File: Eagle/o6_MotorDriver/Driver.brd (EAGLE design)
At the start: 160 x 100 mm, 17 parts, among them IC1 ULN2003AD, IC2 REG1117, P1C2 10uF, P1C3 10uF

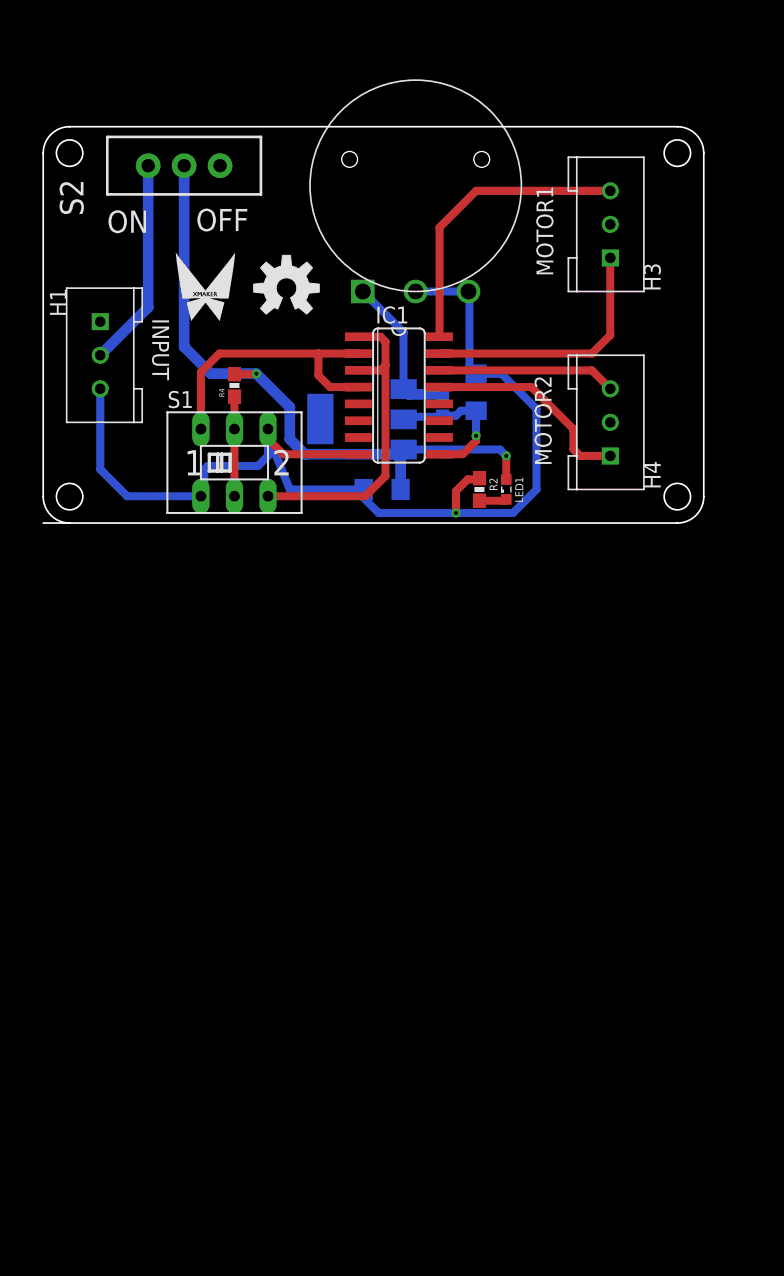
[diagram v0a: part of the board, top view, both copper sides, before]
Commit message: change motordriver
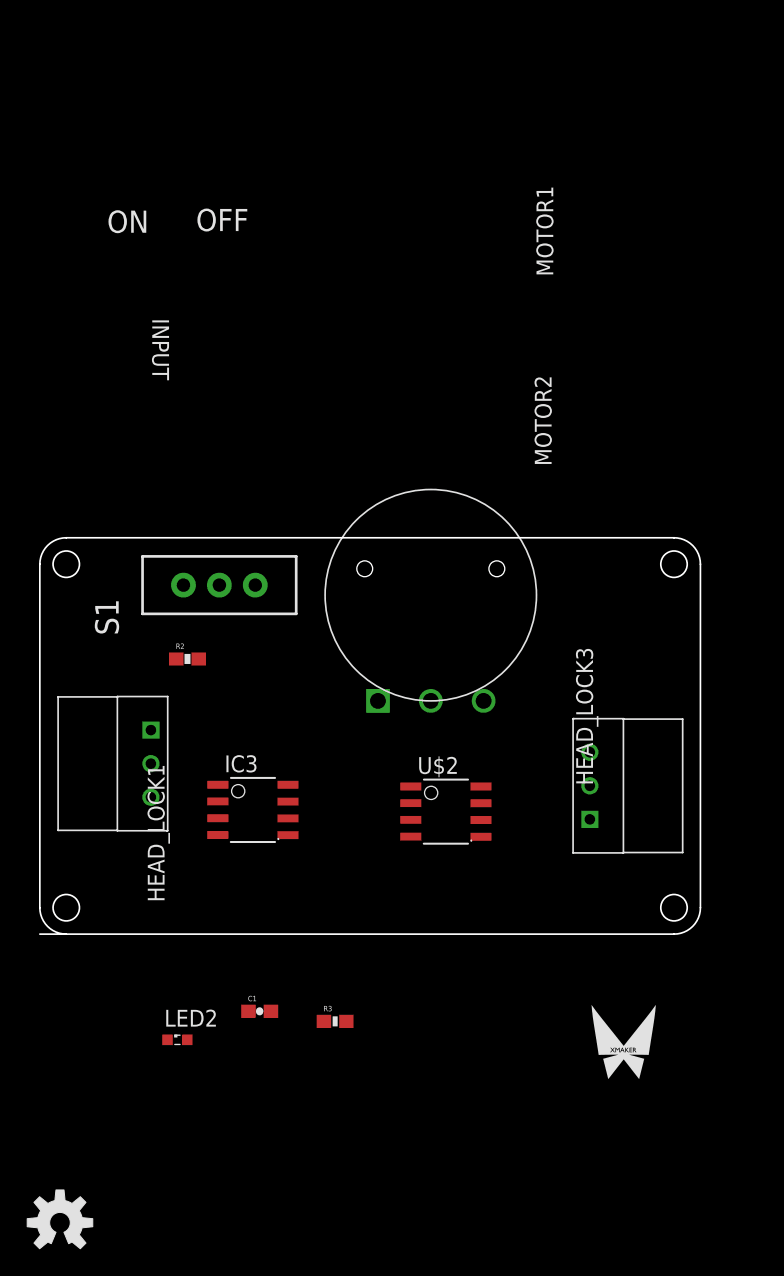
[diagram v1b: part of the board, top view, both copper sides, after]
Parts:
- removed H1, H3, H4: HEAD_LOCK, HEAD_LOCK:HEAD_LOCK
- removed IC1: ULN2003AD, uln-udn:SO16
- removed IC2: REG1117, burr-brown:SOT223
- removed LED1: (no value), eagle-ltspice:LED_SML0603
- removed P1C2, P1C3: 10uF, SparkFun:EIA3216
- removed R1: 121, SparkFun-Resistors:0603-RES
- removed R4: 10K, SparkFun-Resistors:0603-RES
- removed S2: (no value), SparkFun-Electromechanical:SWITCH-SPDT_KIT
- removed U$3: DIMENSION1, Xmaker_yuhui:DIMENSION1
- removed U$4: OPENHARDWARE, Xmaker_yuhui:OPENHARDWARE
- removed U$5: 1K, Xmaker_yuhui:POT_CIRCLE
- added C1: 0.1uF, SparkFun-Passives:0603-CAP
- added HEAD_LOCK1, HEAD_LOCK3: HEAD_LOCK, Xmaker_yuhui:HEAD_LOCK
- added IC3: TINY13-20SSU, atmel:8S1
- added LED2: (no value), eagle-ltspice:LED_SML0603
- added R3: (no value), SparkFun-Resistors:0603-RES
- added U$1: DIMENSION1, Xmaker_yuhui:DIMENSION1
- added U$6: POL_CIRCLE, Xmaker_yuhui:POT_CIRCLE
- added U$7: XMAKERLOGO_5MM_TOP, Xmaker_yuhui:XMAKERLOGO_5MM_TOP
- added U$8: OPENHARDWARE_5MM_TOP, Xmaker_yuhui:OPENSOURCE_5MM_TOP
- R2: device SparkFun-Resistors:0603-RES -> SparkFun-Passives:0603-RES
- S1: device switch:A68-A31 -> SparkFun-Electromechanical:SWITCH-SPDT_KIT
- U$2: value XMAKERLOGO2 -> L9110; device Xmaker_yuhui:XMAKERLOGO2 -> Xmaker_yuhui:SOP8
- moved U$2 42.2 mm to (31.8, -62.5), turned to 270 degrees
- moved R2 25.6 mm to (12.2, -50.9), turned to 0 degrees
- moved S1 9.34 mm to (14.6, -45.3), turned to 90 degrees
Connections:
- removed net IN1: IC1.1, IC1.3, S1.3
- removed net IN2: IC1.2, IC1.4, S1.4
- removed net MOTOR3: H4.1, IC1.13
- removed net MOTOR4: H4.3, IC1.14
- removed net N$1: LED1.C, R2.2
- removed net N$3: IC2.1, R1.1, U$5.P$1
- removed net N$4: H1.2, S2.1
- removed net VOUT: IC1.9, IC2.2, P1C3.A, R1.2
- new net ADC: HEAD_LOCK1.1, IC3.2
- new net DIR: IC3.7, U$2.7
- new net N$5: LED2.C, R3.2
- new net PWM: IC3.5, U$2.6
- new net SELECT: IC3.6, S1.2
- new net SPEED: IC3.3, U$6.P$2
- net GND: now also C1.2, HEAD_LOCK1.3, IC3.4, R3.1, S1.3, U$2.5, U$2.8, U$6.P$3; no longer H1.3, IC1.8, P1C2.C, P1C3.C, R2.1, S1.1, S1.6, U$5.P$2, U$5.P$3
- net MOTOR1: now also HEAD_LOCK3.3, U$2.1; no longer H3.1, IC1.15
- net MOTOR2: now also HEAD_LOCK3.1, U$2.4; no longer H3.3, IC1.16
- net N$2: now also R2.1, S1.1; no longer R4.1, S1.2, S1.5
- net VCC: now also C1.1, HEAD_LOCK1.2, IC3.1, IC3.8, LED2.A, R2.2, U$2.2, U$2.3, U$6.P$1; no longer IC2.3, LED1.A, P1C2.A, R4.2, S2.2
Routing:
- net GND: track 82.9 -> 0.00 mm, vias 1 -> 0
- net VCC: track 48.8 -> 0.00 mm, vias 2 -> 0
- net IN1: track 24.1 -> 0.00 mm
- net MOTOR2: track 22.4 -> 0.00 mm
- net IN2: track 21.9 -> 0.00 mm
- net MOTOR1: track 19.3 -> 0.00 mm
- net MOTOR3: track 16.0 -> 0.00 mm
- net N$4: track 15.9 -> 0.00 mm
- net MOTOR4: track 13.5 -> 0.00 mm
- net N$3: track 11.8 -> 0.00 mm
- net VOUT: track 11.2 -> 0.00 mm, vias 1 -> 0
- net N$2: track 7.53 -> 0.00 mm
- net N$1: track 2.07 -> 0.00 mm

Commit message: gxzz
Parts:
- moved LED2 45.3 mm to (43.7, -48.0), turned to 180 degrees
- moved R3 35.3 mm to (44.2, -49.9)
- moved C1 19.3 mm to (18.4, -58.3)
- moved U$8 11.5 mm to (9.53, -84.5)
- moved IC3 3.18 mm to (20.3, -62.5)
- moved R2 2.33 mm to (10.0, -50.0), turned to 270 degrees
- moved HEAD_LOCK3 2.05 mm to (42.4, -58.5)
- moved S1 1.91 mm to (12.7, -45.5)
- moved U$6 0.90 mm to (30.0, -54.7)
- moved HEAD_LOCK1 0.72 mm to (9.91, -58.3)

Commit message: 12.15
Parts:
- removed HEAD_LOCK1, HEAD_LOCK3: HEAD_LOCK, Xmaker_yuhui:HEAD_LOCK
- added HEAD_LOCK2: HEAD_LOCK, Xmaker:HEAD_LOCK
- added U$4: HEAD_LOCK2, Xmaker:HEAD_LOCK2
- moved U$8 109.5 mm to (9.00, 25.0)
- moved U$7 105.2 mm to (41.0, 25.0)
- moved U$2 73.0 mm to (30.2, 10.5)
- moved LED2 73.0 mm to (45.2, 25.0)
- moved IC3 73.0 mm to (20.8, 10.5)
- moved R3 72.0 mm to (45.7, 22.1)
- moved U$6 71.9 mm to (25.0, 17.0)
- moved U$1 71.8 mm to (0.00, 0.03)
- moved C1 64.6 mm to (19.1, 6.33), turned to 180 degrees
- moved R2 55.0 mm to (10.5, 4.93)
- moved S1 49.5 mm to (25.0, 2.50), turned to 270 degrees
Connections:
- net ADC: now also HEAD_LOCK2.1; no longer HEAD_LOCK1.1
- net GND: now also HEAD_LOCK2.3; no longer HEAD_LOCK1.3
- net MOTOR1: now also U$4.2; no longer HEAD_LOCK3.3
- net MOTOR2: now also U$4.1; no longer HEAD_LOCK3.1
- net VCC: now also HEAD_LOCK2.2; no longer HEAD_LOCK1.2
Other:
- board size 160 x 100 mm -> 50 x 30 mm
